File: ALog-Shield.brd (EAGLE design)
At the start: 53.3 x 78.5 mm, 27 parts, among them U1 DS3231MZ/V+T

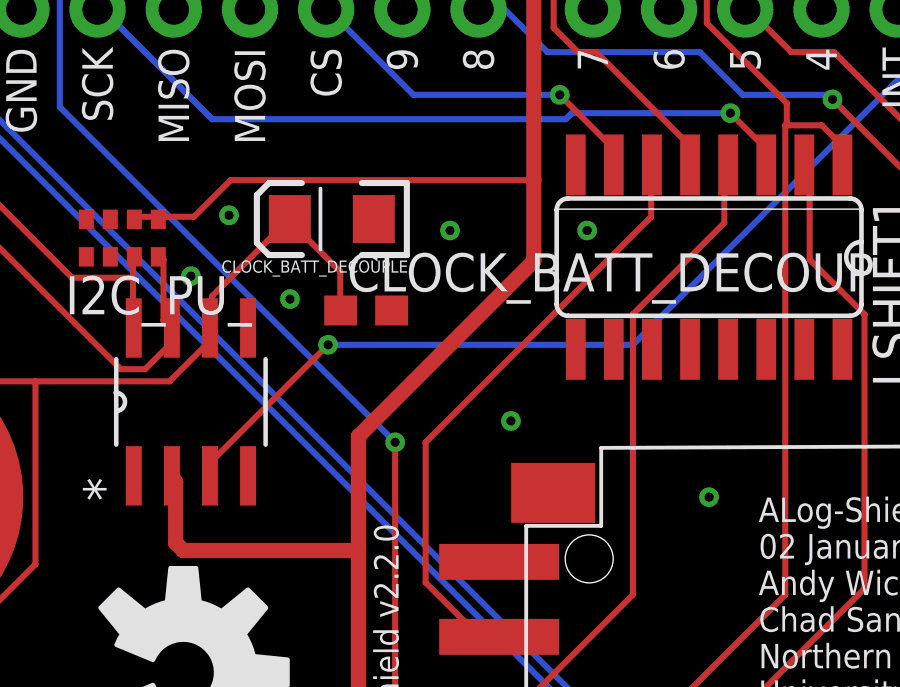
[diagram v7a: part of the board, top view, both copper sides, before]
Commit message: 1206-->0805 10uF, rm floating vias
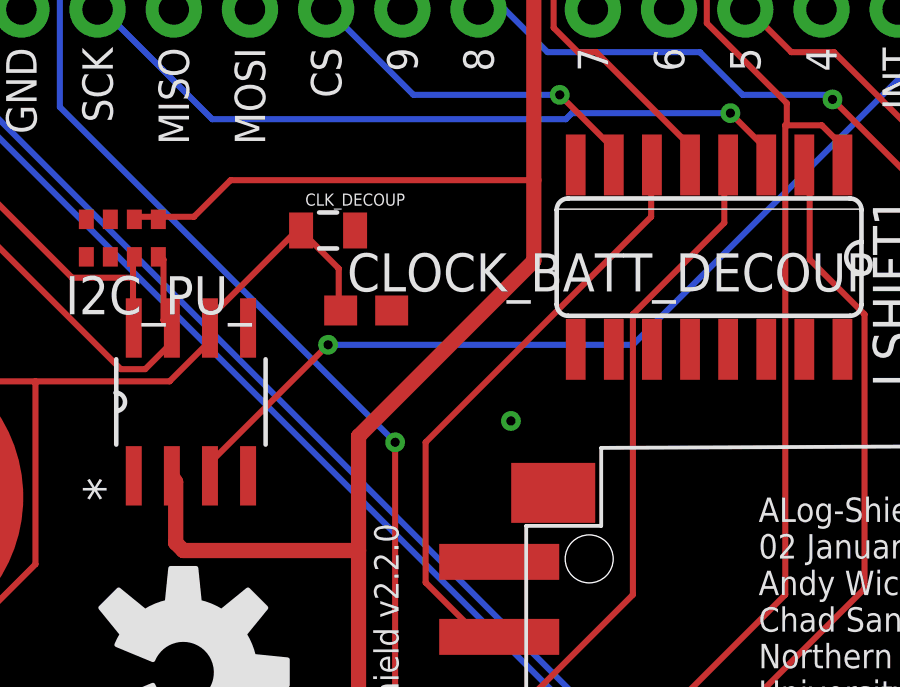
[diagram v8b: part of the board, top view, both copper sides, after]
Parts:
- removed CLOCK_BATT_DECOUPLE: 10uF, SparkFun-Passives:EIA3216
- added CLK_DECOUP: 10 uF, SparkFun-Passives:0805
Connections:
- net BAT: now also CLK_DECOUP.1; no longer CLOCK_BATT_DECOUPLE.A
- net GND: now also CLK_DECOUP.2; no longer CLOCK_BATT_DECOUPLE.C
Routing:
- net BAT: track 36.3 -> 35.6 mm
- net GND: vias 8 -> 2
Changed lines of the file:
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@@
 <attribute name="PROD_ID" value=" SWCH-08441" x="-179.705" y="172.72" size="1.778" layer="27" rot="R270" display="off"/>
 </element>
-<element name="CLOCK_BATT_DECOUPLE" library="SparkFun-Passives" package="EIA3216" value="10uF" x="21.463" y="54.991" rot="R180"/>
 <element name="U1" library="Maxim-DS3231MZ_8-SOIC" package="21-0041B_8" value="DS3231MZ/V+T" x="16.764" y="48.895" rot="R90">
 <attribute name="MANUFACTURER_NAME" value="Maxim" x="315.214" y="-26.035" size="1.778" layer="27" rot="R90" display="off"/>
@@
 </element>
 <element name="U$1" library="awickert" package="NWLOGO_MED" value="NWLOGO_MED" x="7.874" y="67.818" rot="MR0"/>
+<element name="CLK_DECOUP" library="SparkFun-Passives" package="0805" value="10 uF" x="21.336" y="54.61"/>
 </elements>
 <signals>
@@
 <contactref element="LOG" pad="1"/>
 <contactref element="CLOCK_BATT_DECOUP" pad="2"/>
-<contactref element="CLOCK_BATT_DECOUPLE" pad="C"/>
 <contactref element="J1" pad="2"/>
 <contactref element="J2" pad="1"/>
@@
 <vertex x="54.61" y="78.74"/>
 </polygon>
-<via x="20.066" y="52.324" extent="1-16" drill="0.3048" shape="octagon"/>
 <via x="27.432" y="48.26" extent="1-16" drill="0.3048" shape="octagon"/>
-<via x="18.034" y="55.118" extent="1-16" drill="0.3048" shape="octagon"/>
-<via x="34.036" y="45.72" extent="1-16" drill="0.3048" shape="octagon"/>
 <wire x1="23.368" y1="52.2224" x2="23.456" y2="51.943" width="0.2032" layer="1"/>
 <contactref element="C15" pad="D2"/>
@@
 <contactref element="C15" pad="A2"/>
 <via x="10.414" y="26.416" extent="1-16" drill="0.3048" shape="octagon"/>
-<via x="16.764" y="53.086" extent="1-16" drill="0.3048" shape="octagon"/>
 <contactref element="CLOCK_BATT" pad="GND"/>
-<via x="25.4" y="54.61" extent="1-16" drill="0.3048" shape="octagon"/>
 <wire x1="9.5504" y1="29.2608" x2="9.6140125" y2="29.2418" width="0.2032" layer="1"/>
-<via x="29.972" y="54.61" extent="1-16" drill="0.3048" shape="octagon"/>
+<contactref element="CLK_DECOUP" pad="2"/>
 </signal>
 <signal name="VCC">
@@
 <signal name="BAT">
 <contactref element="CLOCK_BATT_DECOUP" pad="1"/>
-<contactref element="CLOCK_BATT_DECOUPLE" pad="A"/>
 <contactref element="U1" pad="6"/>
-<wire x1="21.7424" y1="53.2384" x2="21.7424" y2="52.0192" width="0.2032" layer="1"/>
-<wire x1="20.1168" y1="54.864" x2="21.7424" y2="53.2384" width="0.2032" layer="1"/>
-<wire x1="21.7424" y1="52.0192" x2="21.756" y2="51.943" width="0.2032" layer="1"/>
-<wire x1="20.1168" y1="54.864" x2="20.063" y2="54.991" width="0.2032" layer="1"/>
-<wire x1="17.4752" y1="52.4256" x2="17.4752" y2="51.4096" width="0.2032" layer="1"/>
-<wire x1="19.9136" y1="54.864" x2="17.4752" y2="52.4256" width="0.2032" layer="1"/>
-<wire x1="17.4752" y1="51.4096" x2="17.399" y2="51.3588" width="0.2032" layer="1"/>
-<wire x1="19.9136" y1="54.864" x2="20.063" y2="54.991" width="0.2032" layer="1"/>
 <contactref element="CLOCK_BATT" pad="POWER0"/>
 <contactref element="CLOCK_BATT" pad="POWER1"/>
@@
 <wire x1="11.5824" y1="49.5808" x2="11.5824" y2="43.4848" width="0.2032" layer="1"/>
 <wire x1="6.096" y1="38.2016" x2="6.096" y2="38.1" width="0.2032" layer="1"/>
+<contactref element="CLK_DECOUP" pad="1"/>
+<wire x1="21.6916" y1="53.34" x2="21.6916" y2="52.0954" width="0.2032" layer="1"/>
+<wire x1="20.447" y1="54.5846" x2="21.6916" y2="53.34" width="0.2032" layer="1"/>
+<wire x1="21.6916" y1="52.0954" x2="21.756" y2="51.943" width="0.2032" layer="1"/>
+<wire x1="20.447" y1="54.5846" x2="20.436" y2="54.61" width="0.2032" layer="1"/>
+<wire x1="17.4244" y1="51.7398" x2="20.2692" y2="54.5846" width="0.2032" layer="1"/>
+<wire x1="17.4244" y1="51.3842" x2="17.4244" y2="51.7398" width="0.2032" layer="1"/>
+<wire x1="20.2692" y1="54.5846" x2="20.436" y2="54.61" width="0.2032" layer="1"/>
+<wire x1="17.4244" y1="51.3842" x2="17.399" y2="51.3588" width="0.2032" layer="1"/>
 </signal>
 <signal name="A0">
